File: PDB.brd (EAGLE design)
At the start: 159.7 x 151.3 mm, 76 parts, among them IC1 LM555N

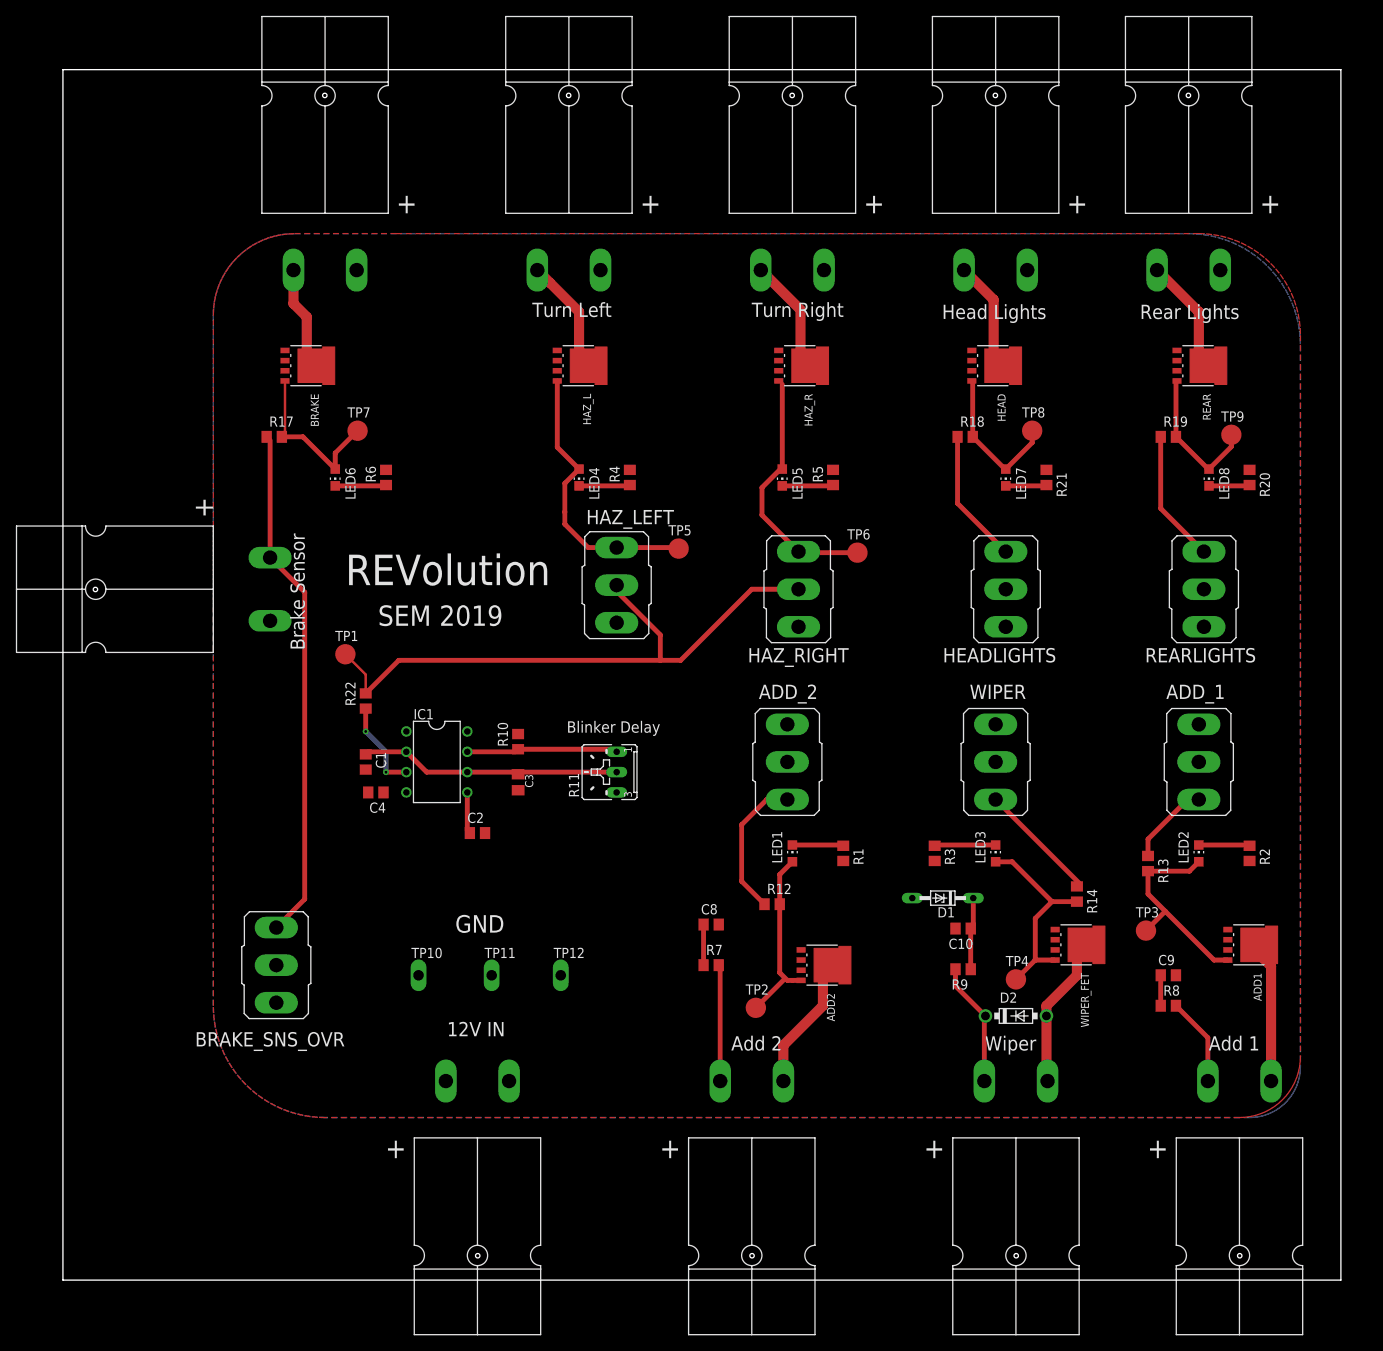
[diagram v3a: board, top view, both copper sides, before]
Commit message: changed GND of brake sensor to VDD
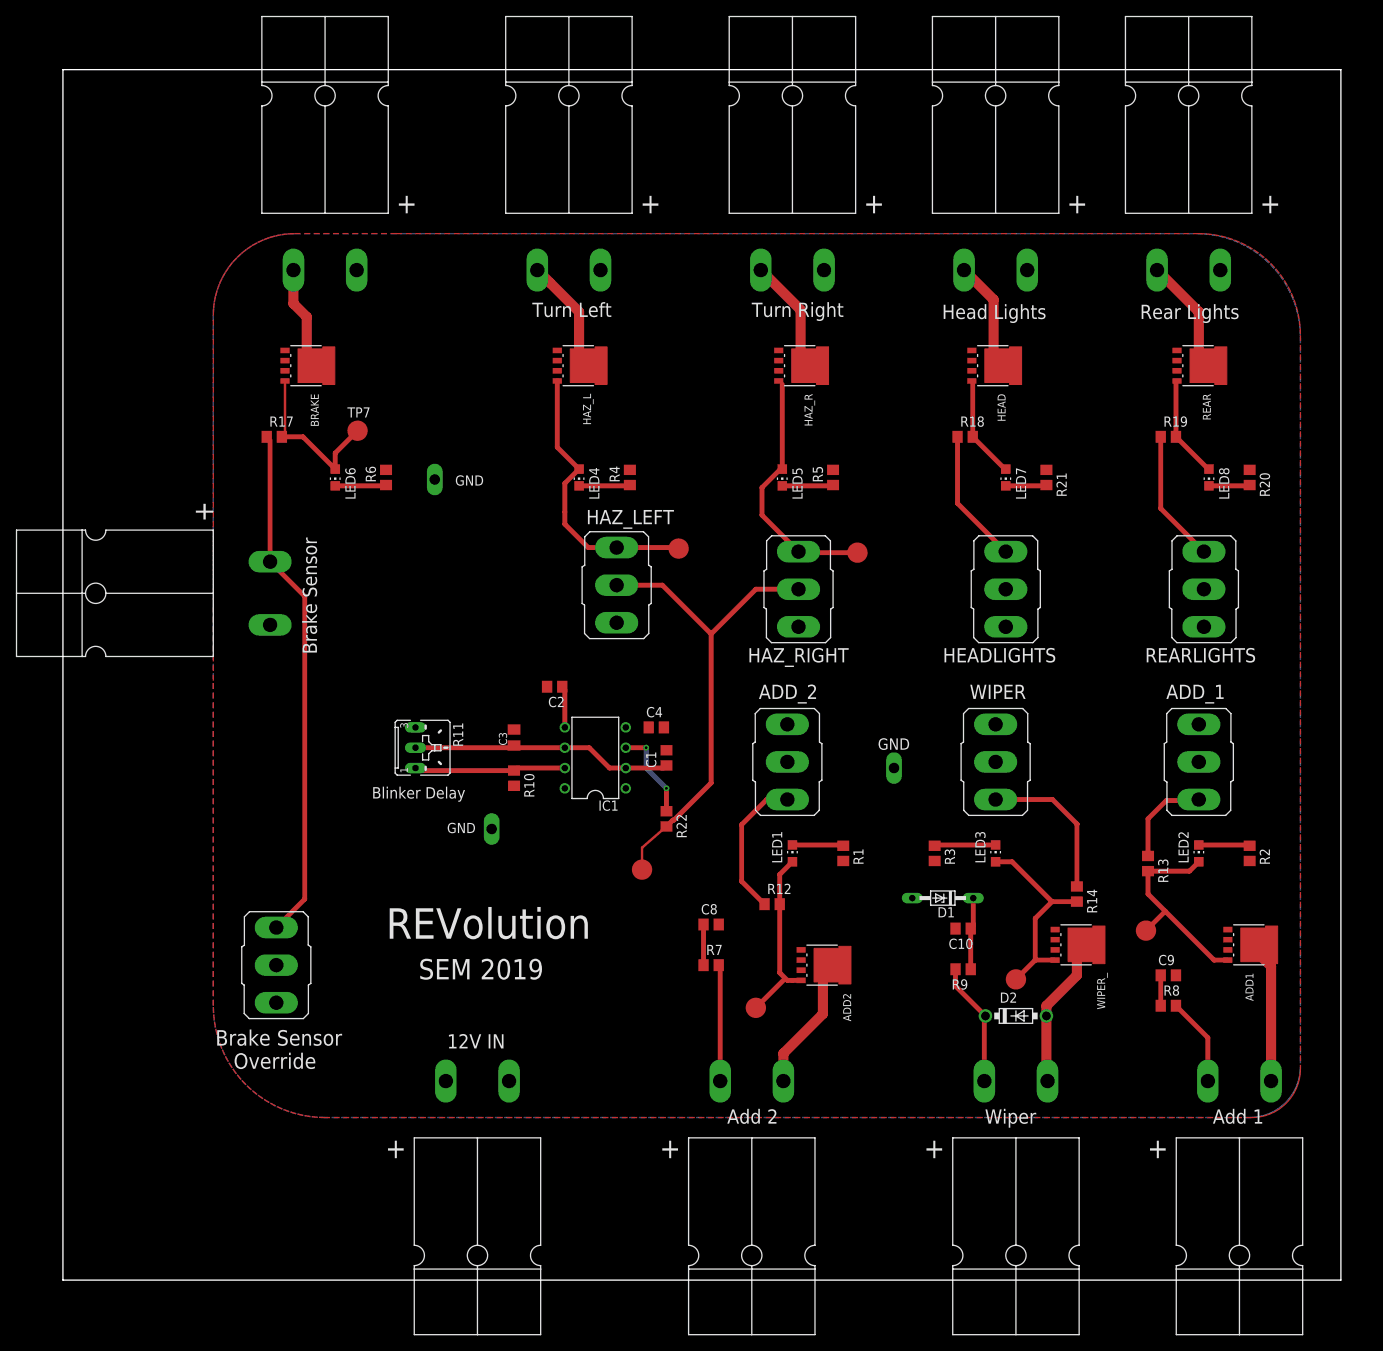
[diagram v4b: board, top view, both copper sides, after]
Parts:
- removed TP8, TP9: PTR1B2,54, testpad:B2,54
- moved TP10 62.0 mm to (44.2, 77.2)
- moved TP11 56.6 mm to (101.6, 41.1)
- moved TP1 45.8 mm to (70.1, 28.4)
- moved R22 40.4 mm to (73.2, 34.8), turned to 270 degrees
- moved C1 37.6 mm to (73.2, 42.4), turned to 90 degrees
- moved C4 36.0 mm to (71.9, 46.2), turned to 0 degrees
- moved R11 23.6 mm to (42.7, 43.7), turned to 270 degrees
- moved C2 20.7 mm to (59.2, 51.3), turned to 180 degrees
- moved TP12 20.2 mm to (51.3, 33.5)
- moved IC1 19.8 mm to (64.3, 42.4), turned to 90 degrees
- moved C3 5.61 mm to (54.1, 45.0), turned to 90 degrees
- moved R10 4.60 mm to (54.1, 39.9), turned to 270 degrees
- moved VDD_IN1 0.51 mm to (16.5, 63.0)
- renumbered WIPER_FET to WIPER_
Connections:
- net GND: no longer VDD_IN1.BLACK
- net N$14: no longer TP8.TP
- net N$15: no longer TP9.TP
- net VDD: now also VDD_IN1.BLACK
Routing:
- net 555_OUT: track 77.1 -> 60.8 mm
- net N$14: track 19.0 -> 12.8 mm
- net N$15: track 18.3 -> 12.8 mm
- net H4: track 15.4 -> 19.3 mm
- net H5: track 11.0 -> 12.5 mm
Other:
- board text added: "Brake Sensor Override"

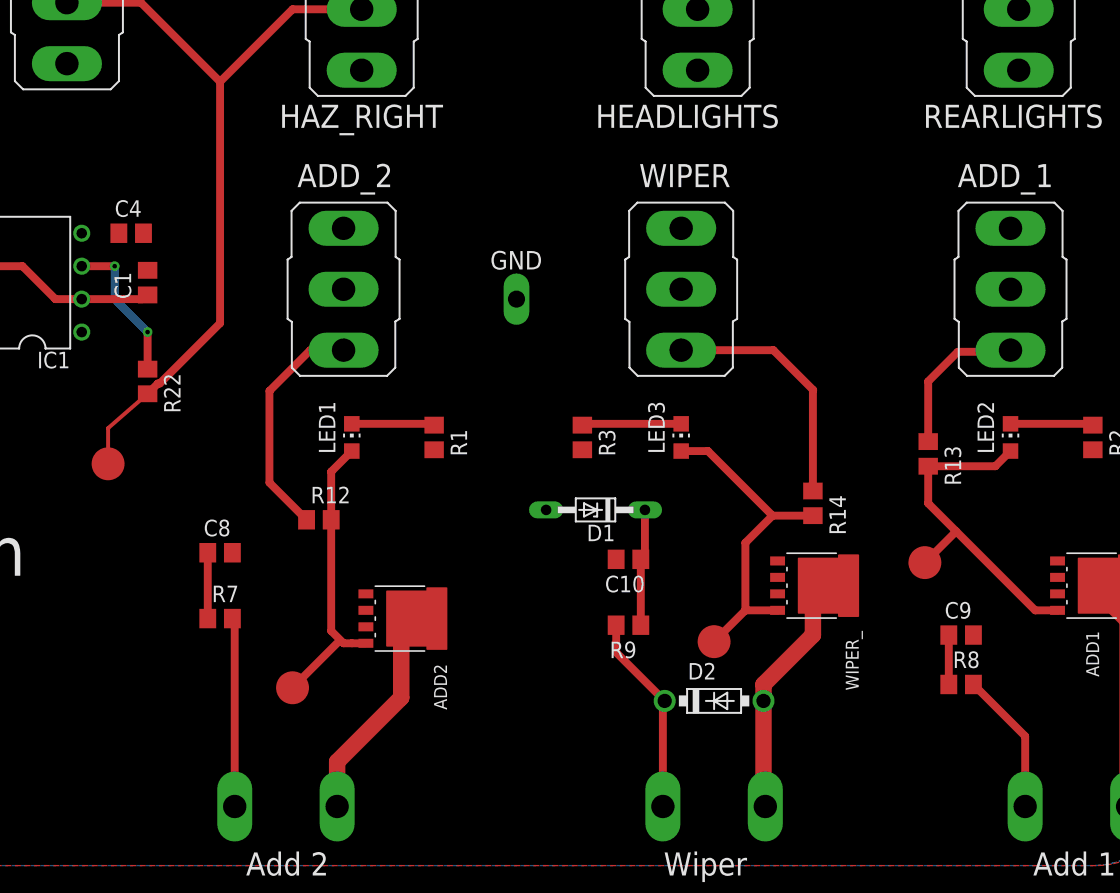
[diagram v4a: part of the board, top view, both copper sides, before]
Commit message: thickened traces
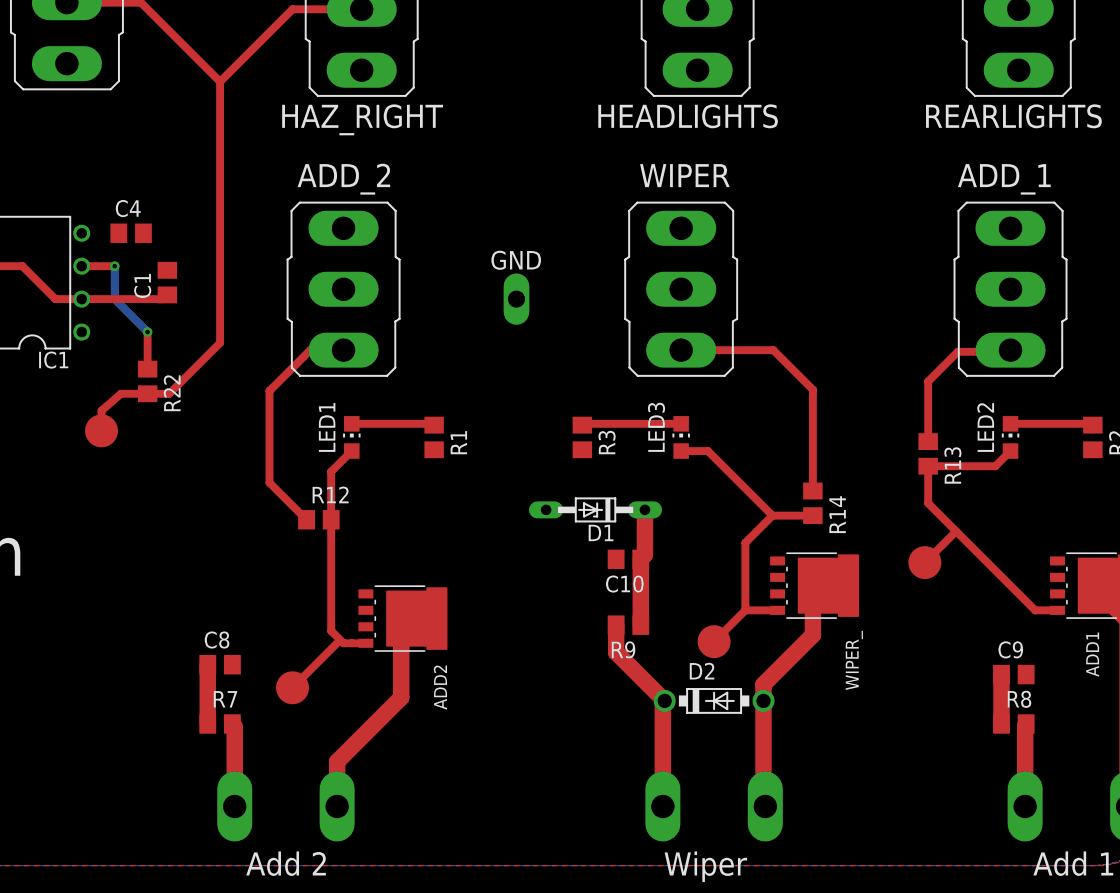
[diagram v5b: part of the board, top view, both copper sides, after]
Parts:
- moved C8 8.64 mm to (78.7, 13.0)
- moved R7 8.13 mm to (78.7, 8.38)
- moved C9 5.08 mm to (140.0, 12.2)
- moved R8 5.08 mm to (140.0, 8.38)
- moved TP1 2.59 mm to (69.6, 31.0)
- moved C1 1.52 mm to (74.7, 42.4)
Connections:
- removed net VDD_ADD1: C9.1, R8.1
- removed net VDD_ADD2: C8.1, R7.1
- removed net VDD_W: C10.1, D1.C, R9.1
- net VDD: now also C10.1, C8.1, C9.1, D1.C, R7.1, R8.1, R9.1
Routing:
- net VDD: track 0.00 -> 17.4 mm
- net VDD_W: track 9.02 -> 0.00 mm
- net N$16: track 14.6 -> 6.44 mm
- net VDD_ADD2: track 5.08 -> 0.00 mm
- net N$18: track 11.1 -> 6.39 mm
- net VDD_ADD1: track 3.81 -> 0.00 mm
- net TR/THR: track 32.8 -> 34.3 mm

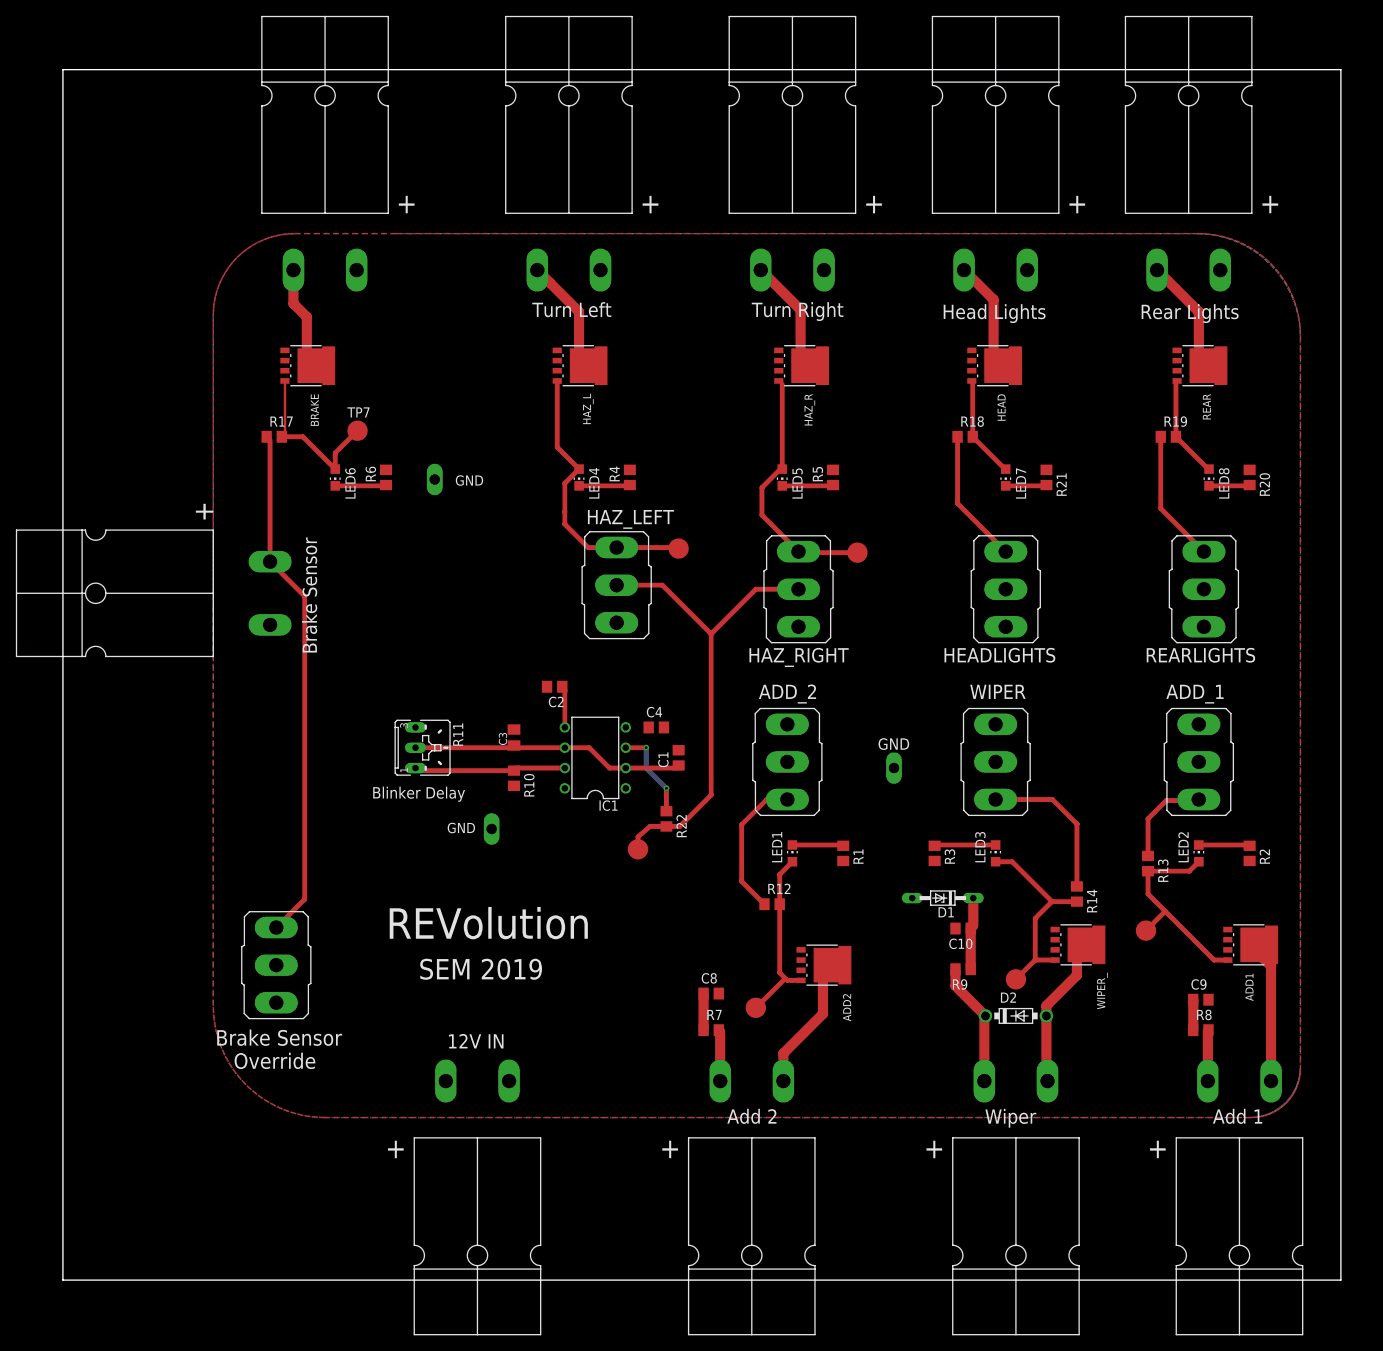
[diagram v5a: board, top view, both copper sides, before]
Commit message: changed switches for Add 1, 2.
made compatible with JST connector
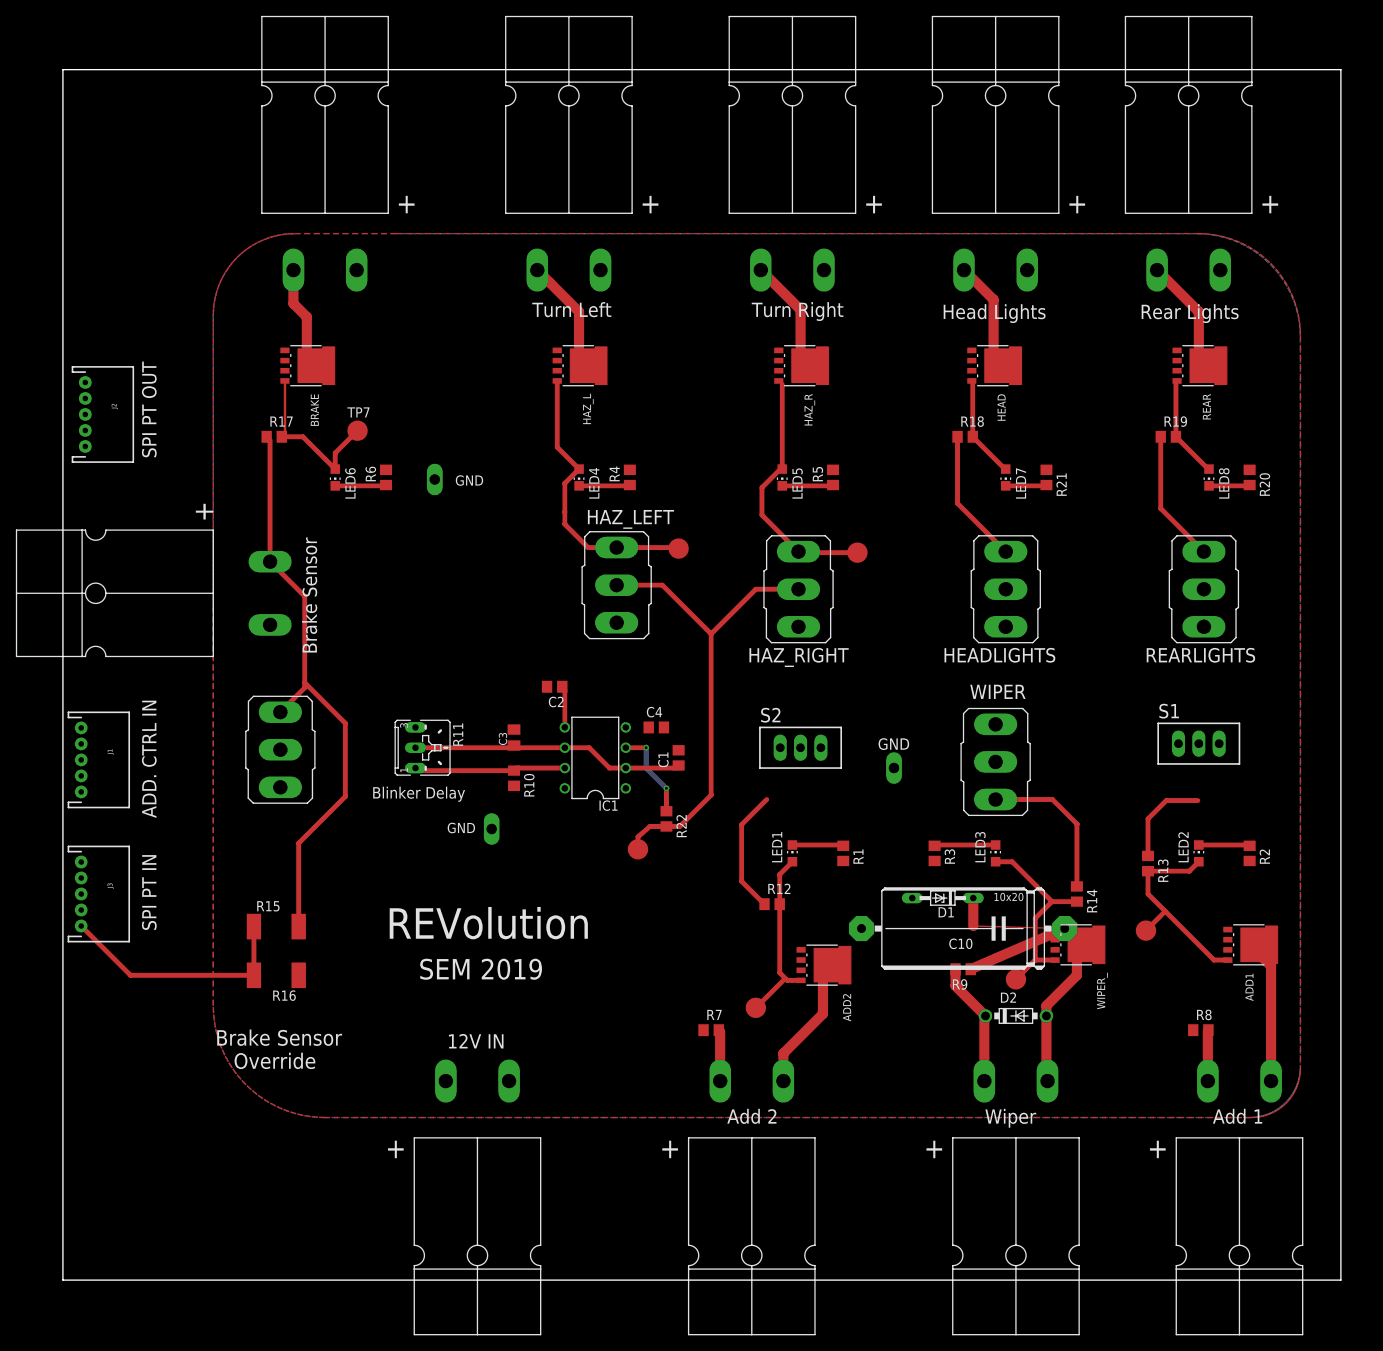
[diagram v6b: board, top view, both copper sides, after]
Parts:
- removed ADD_1, ADD_2: (no value), switch:M9040P
- removed C8, C9: (no value), rcl:C0805
- added J1, J2, J3: (no value), SparkFun-Connectors:JST-5-PTH
- added R15: 12K, resistor:R2512
- added R16: 18K, resistor:R2512
- added S1, S2: TL39PO, switch:TL3XPO
- C10: device rcl:C0805 -> resistor:EU25-10
- moved BRAKE_SNS_OVR 26.9 mm to (24.9, 43.4)
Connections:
- removed net H1: BRAKE_SNS_OVR.1, R17.1, VDD_IN1.RED
- new net BRAKE_SNS_: BRAKE_SNS_OVR.1, R15.2, R17.1, VDD_IN1.RED
- new net BRK_SNS_5V: J1.5, J3.5, R15.1, R16.2
- new net CS_SPI: J1.2, J2.2
- new net MISO_SPI: J1.4, J2.4
- new net MOSI_SPI: J1.3, J2.3
- new net N$12: J2.5
- new net SCL_SPI: J1.1, J2.1
- new net µC_1: J3.3, S1.1
- new net µC_2: J3.4, S2.1
- net GND: now also R16.1; no longer C8.2, C9.2
- net H5: now also S1.2; no longer ADD_1.1
- net H6: now also S2.2; no longer ADD_2.1
- net VDD: now also S1.3, S2.3; no longer ADD_1.2, ADD_2.2, C8.1, C9.1
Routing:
- net BRAKE_SNS_: track 0.00 -> 72.7 mm
- net H1: track 64.8 -> 0.00 mm
- net BRK_SNS_5V: track 0.00 -> 30.2 mm
- net VDD: track 17.4 -> 27.7 mm
- net H6: track 18.1 -> 15.6 mm
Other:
- board text added: "ADD. CTRL IN"
- board text added: "SPI PT IN"
- board text added: "SPI PT OUT"
